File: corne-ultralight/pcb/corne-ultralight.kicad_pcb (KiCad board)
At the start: 2 copper layers, 275.5 x 105.6 mm, 148 parts, among them J2 OLED, J5 Breakaway_Tabs, J7 OLED, SW1 SW_PUSH, SW10 SW_PUSH, SW11 SW_PUSH, SW12 SW_PUSH, SW13 SW_PUSH, SW14 SW_PUSH, SW15 SW_PUSH, SW16 SW_PUSH, SW17 SW_PUSH, SW18 SW_PUSH, SW19 SW_PUSH, SW2 SW_PUSH, SW20 SW_PUSH, SW21 SW_PUSH, SW22 SW_PUSH, SW23 SW_PUSH, SW24 SW_PUSH, SW25 SW_PUSH, SW26 SW_PUSH, SW27 SW_PUSH, SW28 SW_PUSH, SW29 SW_PUSH, SW3 SW_PUSH, SW30 SW_PUSH, SW31 SW_PUSH, SW32 SW_PUSH, SW33 SW_PUSH, SW34 SW_PUSH, SW35 SW_PUSH, SW36 SW_PUSH, SW37 SW_PUSH, SW38 SW_PUSH, SW39 SW_PUSH, SW4 SW_PUSH, SW40 SW_PUSH, SW41 SW_PUSH, SW42 SW_PUSH, SW5 SW_PUSH, SW6 SW_PUSH, SW7 SW_PUSH, SW8 SW_PUSH, SW9 SW_PUSH, U1 ProMicro, U2 ProMicro

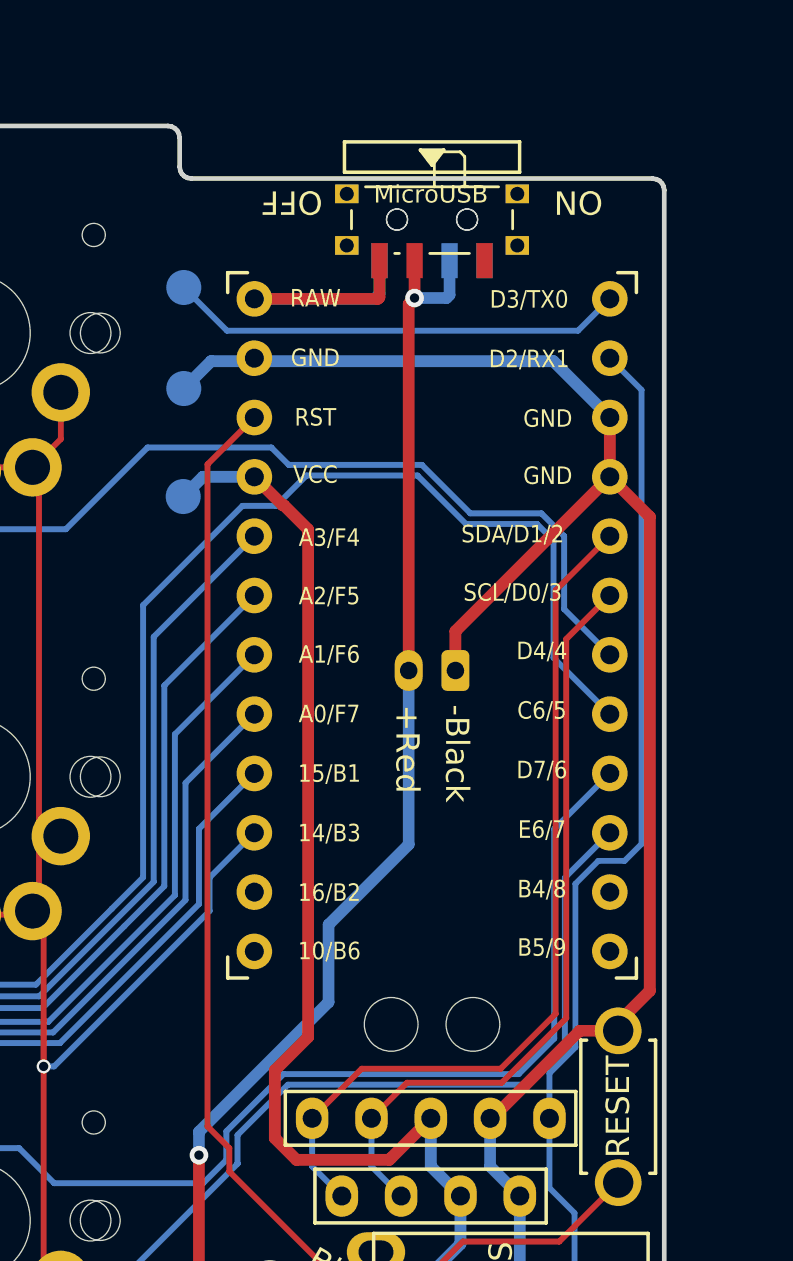
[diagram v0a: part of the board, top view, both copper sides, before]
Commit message: U1 position adjusted
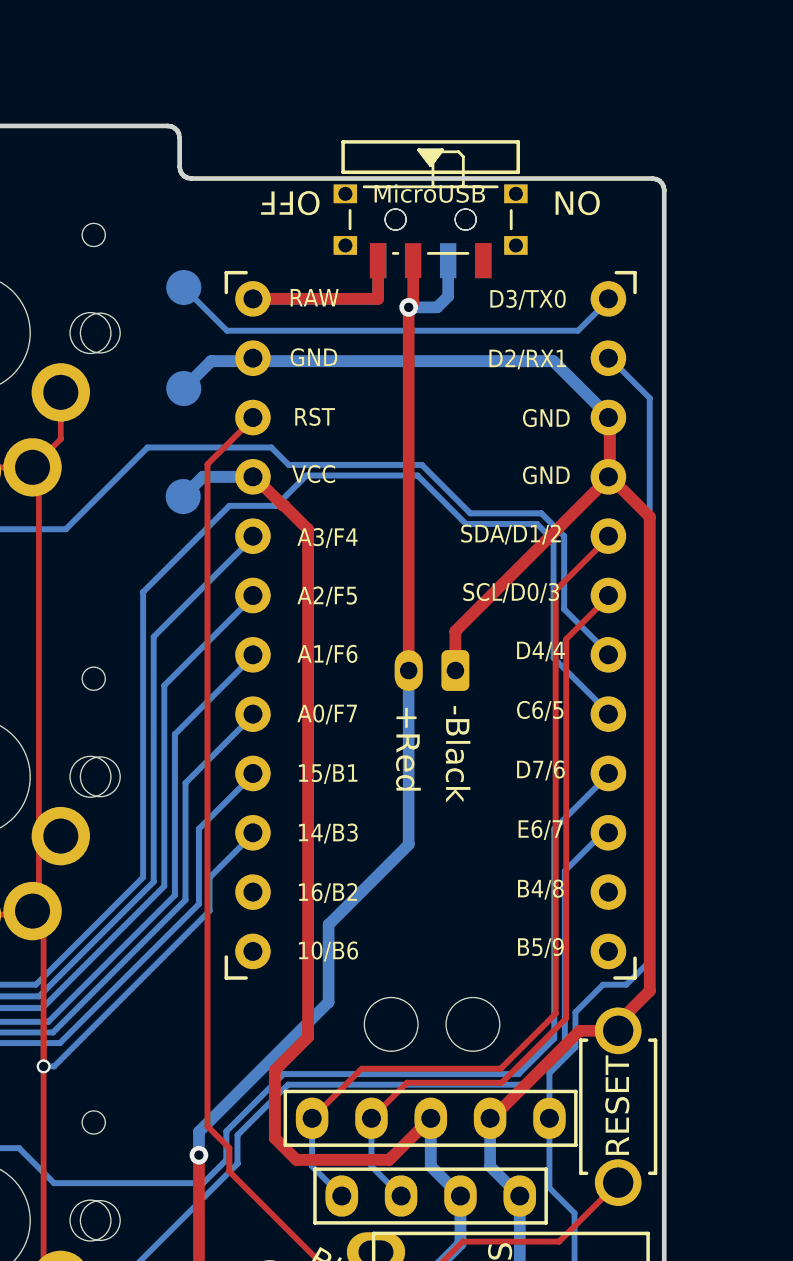
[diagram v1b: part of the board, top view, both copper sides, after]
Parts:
- moved PSW1 0.06 mm to (136.8, 39.0)
- moved PSW3 0.06 mm to (136.8, 39.0)
- moved U1 0.06 mm to (136.8, 56.6)

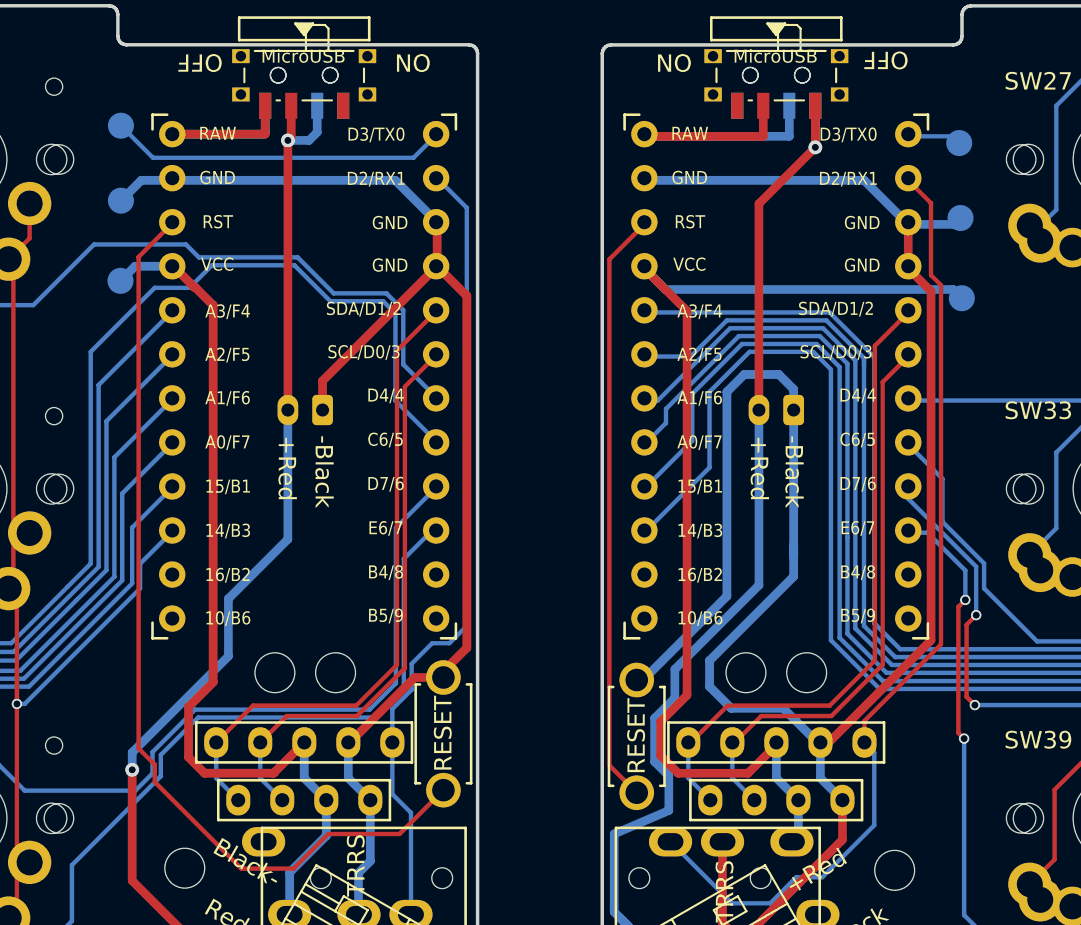
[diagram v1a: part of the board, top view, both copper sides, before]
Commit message: U1 position adjusted
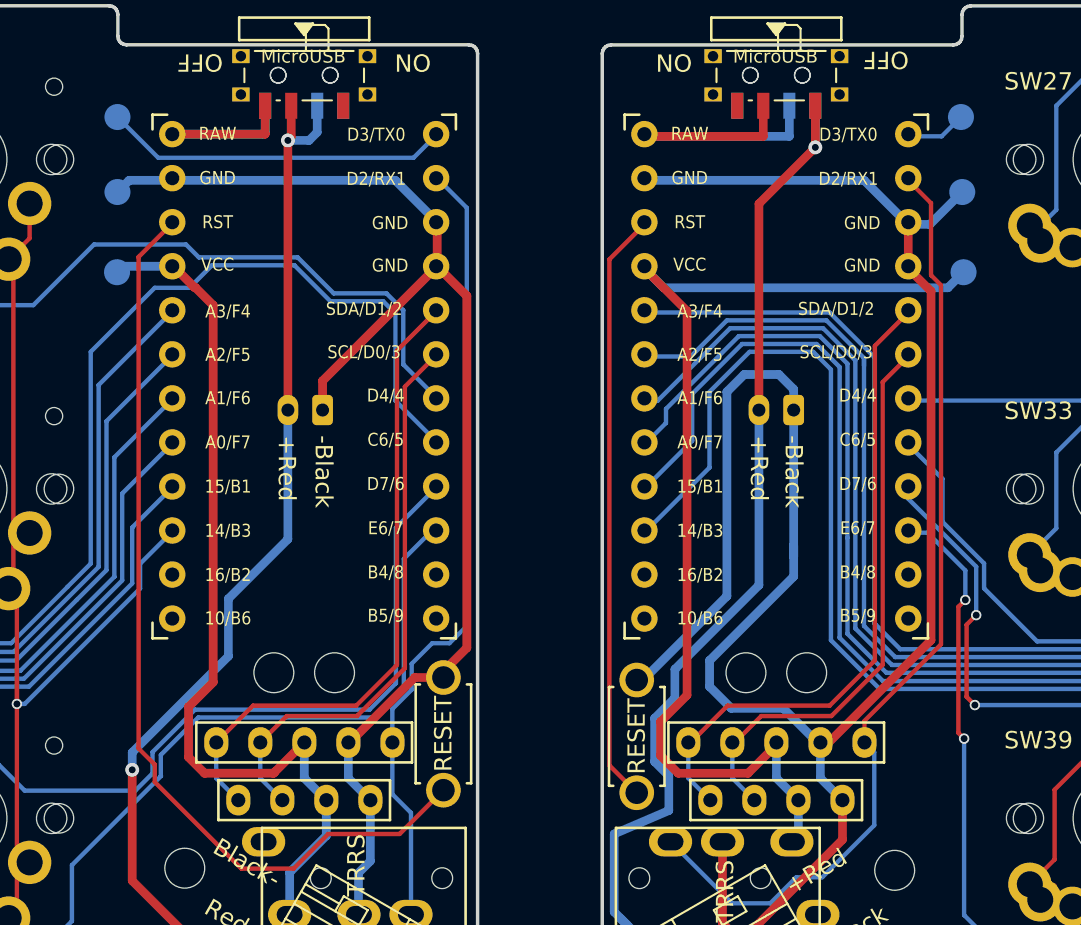
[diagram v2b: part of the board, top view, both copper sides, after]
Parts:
- moved TP5 1.50 mm to (174.9, 50.0)
- moved TP4 1.50 mm to (174.7, 41.1)
- moved TP6 1.50 mm to (174.8, 45.4)
- moved TP1 0.54 mm to (126.1, 41.1)
- moved TP2 0.54 mm to (126.0, 50.0)
- moved TP3 0.54 mm to (126.1, 45.4)
- moved Ref** 0.06 mm to (135.1, 73.1)
- moved Ref** 0.06 mm to (138.6, 73.1)
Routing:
- net RGB_r: track 2.55 -> 3.50 mm
- net GNDA: track 157.1 -> 157.8 mm
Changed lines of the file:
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@@
 	)
 	(footprint "kbd:ProMicro_v3"
+		(locked yes)
 		(layer "F.Cu")
 		(at 136.8325 56.56)
@@
 	(footprint "nice_view:nice_view_1side"
 		(layer "F.Cu")
-		(at 131.7585 77.168)
+		(at 131.7625 77.168)
 		(descr "Connecteur 6 pins")
 		(tags "CONN DEV")
@@
 	(footprint "kbd:thread_m2"
 		(layer "F.Cu")
-		(at 135.1425 73.145)
+		(at 135.0825 73.145)
 		(descr "Mounting Hole 2.2mm, no annular, M2")
 		(tags "mounting hole 2.2mm no annular m2")
@@
 	(footprint "kbd:thread_m2"
 		(layer "F.Cu")
-		(at 138.6425 73.145)
+		(at 138.5825 73.145)
 		(descr "Mounting Hole 2.2mm, no annular, M2")
 		(tags "mounting hole 2.2mm no annular m2")
@@
 	(footprint "kbd:OLED_1side"
 		(layer "F.Cu")
-		(at 133.0285 80.495)
+		(at 133.0325 80.495)
 		(descr "Connecteur 6 pins")
 		(tags "CONN DEV")
@@
 	)
 	(footprint "TestPoint:TestPoint_Pad_D1.5mm"
+		(locked yes)
 		(layer "B.Cu")
-		(at 126.2375 50.545 180)
+		(at 126.0375 50.045 180)
 		(descr "SMD pad as test Point, diameter 1.5mm")
 		(tags "test point SMD pad")
@@
 	)
 	(footprint "TestPoint:TestPoint_Pad_D1.5mm"
+		(locked yes)
 		(layer "B.Cu")
-		(at 174.7625 51.545 180)
+		(at 174.8625 50.045 180)
 		(descr "SMD pad as test Point, diameter 1.5mm")
 		(tags "test point SMD pad")
@@
 	)
 	(footprint "TestPoint:TestPoint_Pad_D1.5mm"
+		(locked yes)
 		(layer "B.Cu")
-		(at 174.6125 42.595 180)
+		(at 174.7125 41.095 180)
 		(descr "SMD pad as test Point, diameter 1.5mm")
 		(tags "test point SMD pad")
@@
 	)
 	(footprint "TestPoint:TestPoint_Pad_D1.5mm"
+		(locked yes)
 		(layer "B.Cu")
-		(at 174.6875 46.92 180)
+		(at 174.7875 45.42 180)
 		(descr "SMD pad as test Point, diameter 1.5mm")
 		(tags "test point SMD pad")
@@
 	)
 	(footprint "TestPoint:TestPoint_Pad_D1.5mm"
+		(locked yes)
 		(layer "B.Cu")
-		(at 126.2625 41.595 180)
+		(at 126.0625 41.095 180)
 		(descr "SMD pad as test Point, diameter 1.5mm")
 		(tags "test point SMD pad")
@@
 	)
 	(footprint "TestPoint:TestPoint_Pad_D1.5mm"
+		(locked yes)
 		(layer "B.Cu")
-		(at 126.2625 45.92 180)
+		(at 126.0625 45.42 180)
 		(descr "SMD pad as test Point, diameter 1.5mm")
 		(tags "test point SMD pad")
@@
 	)
 	(segment
+		(start 126.734068 44.748432)
+		(end 142.090332 44.748432)
+		(width 0.508)
+		(layer "B.Cu")
+		(net 5)
+	)
+	(segment
 		(start 139.9925 86.975)
 		(end 139.9925 87.566187)
@@
 	)
 	(segment
-		(start 142.090332 44.748432)
-		(end 144.5039 47.162)
-		(width 0.508)
-		(layer "B.Cu")
-		(net 5)
-	)
-	(segment
 		(start 131.2125 117.177051)
 		(end 131.480449 117.445)
@@
 	)
 	(segment
-		(start 129.2839 44.748432)
-		(end 142.090332 44.748432)
-		(width 0.508)
-		(layer "B.Cu")
-		(net 5)
-	)
-	(segment
-		(start 126.2625 45.92)
-		(end 127.434068 44.748432)
-		(width 0.508)
-		(layer "B.Cu")
-		(net 5)
-	)
-	(segment
 		(start 139.3785 77.168)
 		(end 139.3785 79.225)
@@
 	)
 	(segment
-		(start 139.3785 79.225)
-		(end 140.6485 80.495)
-		(width 0.5)
+		(start 142.090332 44.748432)
+		(end 144.5039 47.162)
+		(width 0.508)
 		(layer "B.Cu")
 		(net 5)
 	)
 	(segment
-		(start 127.434068 44.748432)
-		(end 129.2839 44.748432)
-		(width 0.508)
+		(start 139.3785 79.225)
+		(end 140.6485 80.495)
+		(width 0.5)
 		(layer "B.Cu")
 		(net 5)
@@
 	)
 	(segment
+		(start 126.0625 45.42)
+		(end 126.734068 44.748432)
+		(width 0.508)
+		(layer "B.Cu")
+		(net 5)
+	)
+	(segment
 		(start 130.1625 75.114)
 		(end 130.1625 78.02)
@@
 	)
 	(segment
-		(start 127.0805 49.702)
-		(end 126.2375 50.545)
-		(width 0.508)
-		(layer "B.Cu")
-		(net 6)
-	)
-	(segment
 		(start 136.8385 79.225)
 		(end 138.1085 80.495)
@@
 	(segment
 		(start 129.2839 49.702)
-		(end 127.0805 49.702)
+		(end 126.3805 49.702)
 		(width 0.508)
 		(layer "B.Cu")
@@
 	)
 	(segment
+		(start 126.3805 49.702)
+		(end 126.0375 50.045)
+		(width 0.508)
+		(layer "B.Cu")
+		(net 6)
+	)
+	(segment
 		(start 25.9975 67.46)
 		(end 25.1625 66.625)
@@
 	)
 	(segment
-		(start 128.1125 43.445)
-		(end 126.2625 41.595)
+		(start 143.1409 43.445)
+		(end 128.4125 43.445)
 		(width 0.25)
 		(layer "B.Cu")
@@
 	)
 	(segment
-		(start 143.1409 43.445)
-		(end 128.1125 43.445)
+		(start 128.4125 43.445)
+		(end 126.0625 41.095)
 		(width 0.25)
 		(layer "B.Cu")
@@
 	)
 	(segment
-		(start 157.666247 51.040432)
-		(end 174.257932 51.040432)
+		(start 164.0675 79.225)
+		(end 165.3375 80.495)
 		(width 0.5)
 		(layer "B.Cu")
@@
 	)
 	(segment
-		(start 164.0675 79.225)
-		(end 165.3375 80.495)
+		(start 156.454247 49.828432)
+		(end 157.570815 50.945)
 		(width 0.5)
 		(layer "B.Cu")
@@
 	)
 	(segment
-		(start 156.454247 49.828432)
-		(end 157.666247 51.040432)
+		(start 165.3375 80.495)
+		(end 165.3375 82.521147)
 		(width 0.5)
 		(layer "B.Cu")
@@
 	)
 	(segment
-		(start 174.257932 51.040432)
-		(end 174.7625 51.545)
+		(start 164.0675 77.168)
+		(end 164.0675 79.225)
 		(width 0.5)
 		(layer "B.Cu")
@@
 	)
 	(segment
-		(start 165.3375 80.495)
-		(end 165.3375 82.521147)
+		(start 173.9625 50.945)
+		(end 174.8625 50.045)
 		(width 0.5)
 		(layer "B.Cu")
@@
 	)
 	(segment
-		(start 164.0675 77.168)
-		(end 164.0675 79.225)
+		(start 157.570815 50.945)
+		(end 173.9625 50.945)
 		(width 0.5)
 		(layer "B.Cu")
@@
 	)
 	(segment
+		(start 171.674247 47.288432)
+		(end 172.919068 47.288432)
+		(width 0.5)
+		(layer "B.Cu")
+		(net 38)
+	)
+	(segment
 		(start 161.2125 68.729779)
 		(end 156.374847 73.567432)
@@
 	)
 	(segment
-		(start 174.319068 47.288432)
-		(end 174.6875 46.92)
-		(width 0.5)
-		(layer "B.Cu")
-		(net 38)
-	)
-	(segment
 		(start 166.6075 79.225)
 		(end 167.8775 80.495)
@@
 	)
 	(segment
-		(start 167.8775 80.495)
-		(end 167.8775 81.245)
+		(start 172.919068 47.288432)
+		(end 174.7875 45.42)
 		(width 0.5)
 		(layer "B.Cu")
@@
 	)
 	(segment
-		(start 171.674247 47.288432)
-		(end 174.319068 47.288432)
+		(start 167.8775 80.495)
+		(end 167.8775 81.245)
 		(width 0.5)
 		(layer "B.Cu")
@@
 	)
 	(segment
+		(start 173.599068 42.208432)
+		(end 174.7125 41.095)
+		(width 0.25)
+		(layer "B.Cu")
+		(net 43)
+	)
+	(segment
 		(start 171.674247 42.208432)
-		(end 174.225932 42.208432)
+		(end 173.599068 42.208432)
 		(width 0.25)
 		(layer "B.Cu")
@@
 		)
 	)
+	(group ""
+		(locked yes)
+		(members "4a5dcc68-6dc6-4e0e-b856-4b50c45721b2" "9e336f04-4f2e-4812-98f8-27e4758a2561"
+			"be8b1a13-f160-41f4-bf4f-60c120156153"
+		)
+	)
+	(group ""
+		(locked yes)
+		(members "3eb7c0fd-b177-4ece-a2a1-c1bdb113673e" "e9a5e6cc-f3df-4920-ac66-755f6a28c62b"
+			"fe935cb6-7ec4-4496-af7c-532ee84bd092"
+		)
+	)

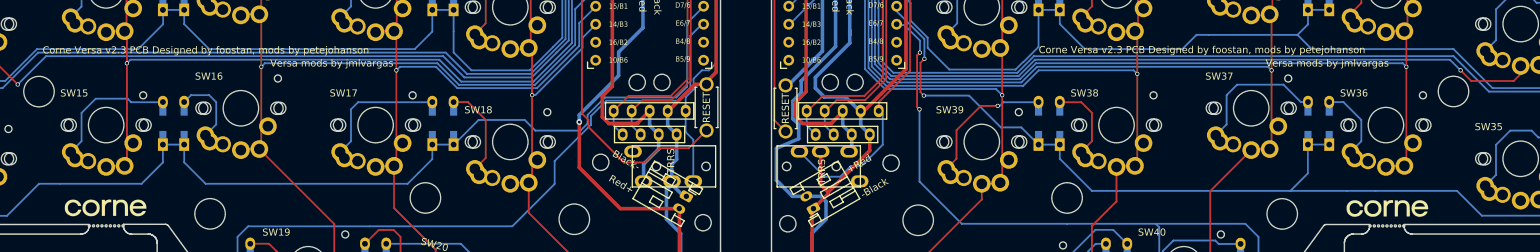
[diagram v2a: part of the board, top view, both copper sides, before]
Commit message: Bottom plate, space for rubber feet
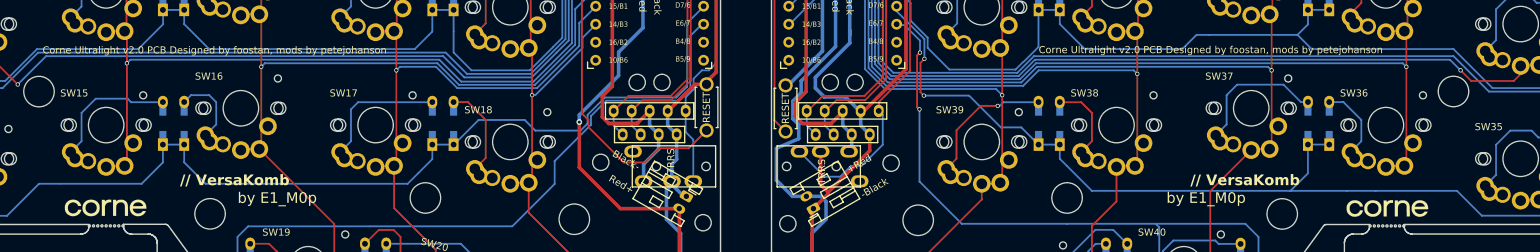
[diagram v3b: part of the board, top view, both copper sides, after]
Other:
- board text added: "// VersaKomb"
- board text added: "Corne Ultralight v2.0 PCB Designed by foostan, mods by petejohanson"
- board text added: "by E1_M0p"
- board text removed: "Corne Versa v2.3 PCB Designed by foostan, mods by petejohanson"
- board text removed: "Versa mods by jmlvargas"
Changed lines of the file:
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@@
 	)
 	(footprint "gateron-ks27:gateron-ks27-choc-v1-mx"
+		(locked yes)
 		(layer "F.Cu")
 		(at 221.684847 76.795432)
@@
 	)
 	(footprint "gateron-ks27:gateron-ks27-choc-v1-mx"
+		(locked yes)
 		(layer "F.Cu")
 		(at 79.1875 76.795)
@@
 		)
 	)
+	(gr_text "// VersaKomb"
+		(at 87.546428 86.945 -0)
+		(layer "B.SilkS")
+		(effects
+			(font
+				(size 1.5 1.5)
+				(thickness 0.3)
+				(bold yes)
+			)
+			(justify left mirror)
+		)
+	)
 	(gr_text "OFF"
 		(at 168.8525 38.045 180)
@@
 		)
 	)
+	(gr_text "by E1_M0p"
+		(at 222.2125 89.445 -0)
+		(layer "B.SilkS")
+		(effects
+			(font
+				(size 1.5 1.5)
+				(thickness 0.1875)
+			)
+			(justify left mirror)
+		)
+	)
 	(gr_text "Red+"
 		(at 163.2125 86.57 30)
@@
 		)
 	)
-	(gr_text "Corne Versa v2.3 PCB Designed by foostan, mods by petejohanson"
+	(gr_text "// VersaKomb"
+		(at 230.497296 86.945 -0)
+		(layer "B.SilkS")
+		(effects
+			(font
+				(size 1.5 1.5)
+				(thickness 0.3)
+				(bold yes)
+			)
+			(justify left mirror)
+		)
+	)
+	(gr_text "by E1_M0p"
+		(at 90.7125 89.445 -0)
+		(layer "B.SilkS")
+		(effects
+			(font
+				(size 1.5 1.5)
+				(thickness 0.1875)
+			)
+			(justify left mirror)
+		)
+	)
+	(gr_text "Corne Ultralight v2.0 PCB Designed by foostan, mods by petejohanson"
 		(at 191.7125 68.56 0)
 		(layer "F.SilkS")
@@
 		)
 	)
-	(gr_text "Corne Versa v2.3 PCB Designed by foostan, mods by petejohanson"
+	(gr_text "Corne Ultralight v2.0 PCB Designed by foostan, mods by petejohanson"
 		(at 51.2125 68.6 0)
 		(layer "F.SilkS")
@@
 		)
 	)
+	(gr_text "// VersaKomb"
+		(at 70.601786 86.945 0)
+		(layer "F.SilkS")
+		(effects
+			(font
+				(size 1.5 1.5)
+				(thickness 0.3)
+				(bold yes)
+			)
+			(justify left)
+		)
+	)
 	(gr_text "Black-"
 		(at 131.7125 83.07 -30)
@@
 		)
 	)
+	(gr_text "by E1_M0p"
+		(at 78.7125 89.445 0)
+		(layer "F.SilkS")
+		(effects
+			(font
+				(size 1.5 1.5)
+				(thickness 0.1875)
+			)
+			(justify left)
+		)
+	)
 	(gr_text "Red+"
 		(at 127.2125 112.945 -30)
@@
 		)
 	)
-	(gr_text "Versa mods by jmlvargas"
-		(at 223.7125 70.445 0)
+	(gr_text "// VersaKomb"
+		(at 213.099133 86.945 0)
 		(layer "F.SilkS")
 		(effects
 			(font
-				(size 1 1)
-				(thickness 0.125)
+				(size 1.5 1.5)
+				(thickness 0.3)
+				(bold yes)
 			)
 			(justify left)
@@
 		)
 	)
-	(gr_text "-Black"
-		(at 169.7125 114.945 30)
+	(gr_text "by E1_M0p"
+		(at 209.7125 89.445 0)
 		(layer "F.SilkS")
 		(effects
 			(font
-				(size 1 1)
-				(thickness 0.15)
+				(size 1.5 1.5)
+				(thickness 0.1875)
 			)
 			(justify left)
@@
 	)
 	(gr_text "-Black"
-		(at 137.955 59.445 -90)
+		(at 169.7125 114.945 30)
 		(layer "F.SilkS")
 		(effects
@@
 		)
 	)
-	(gr_text "OFF"
-		(at 132.1525 37.945 180)
+	(gr_text "-Black"
+		(at 137.955 59.445 -90)
 		(layer "F.SilkS")
 		(effects
@@
 		)
 	)
-	(gr_text "Versa mods by jmlvargas"
-		(at 83.3125 70.445 0)
+	(gr_text "OFF"
+		(at 132.1525 37.945 180)
 		(layer "F.SilkS")
 		(effects
 			(font
 				(size 1 1)
-				(thickness 0.125)
+				(thickness 0.15)
 			)
 			(justify left)

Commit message: Updates
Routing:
- net CS_r: track 55.3 -> 55.8 mm
